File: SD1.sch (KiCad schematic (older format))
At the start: 43 parts, among them J103 JST ZH 1.5mm 1x5, J107 FPC PMS, Q101 BSS138, Q102 PDTC114EU,115, SW103 Multidirection_Switch, U102 ER-TFTM028-4, U104 CC2652P, U106 EKMC1691111, U107 MCP23017, U108 BME280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

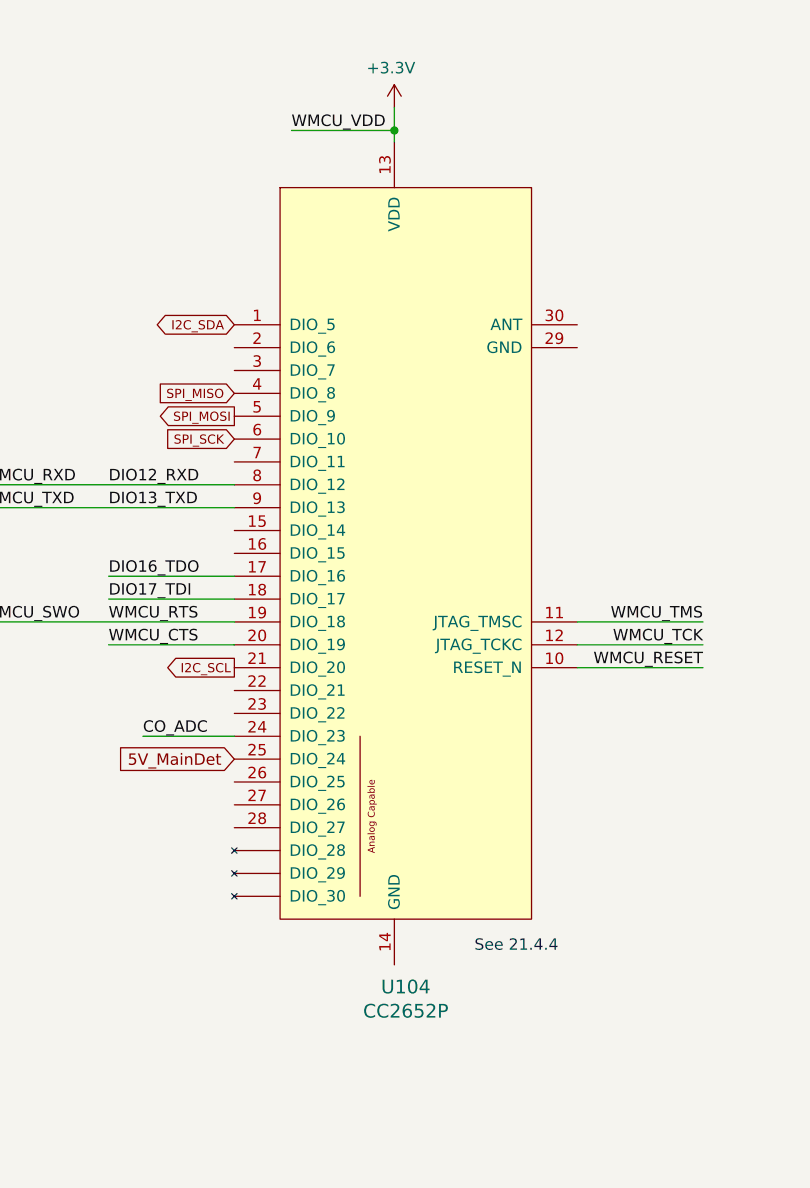
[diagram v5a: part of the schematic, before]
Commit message: PoE layout
Changed opto and fixed ref diode footprint/symbol
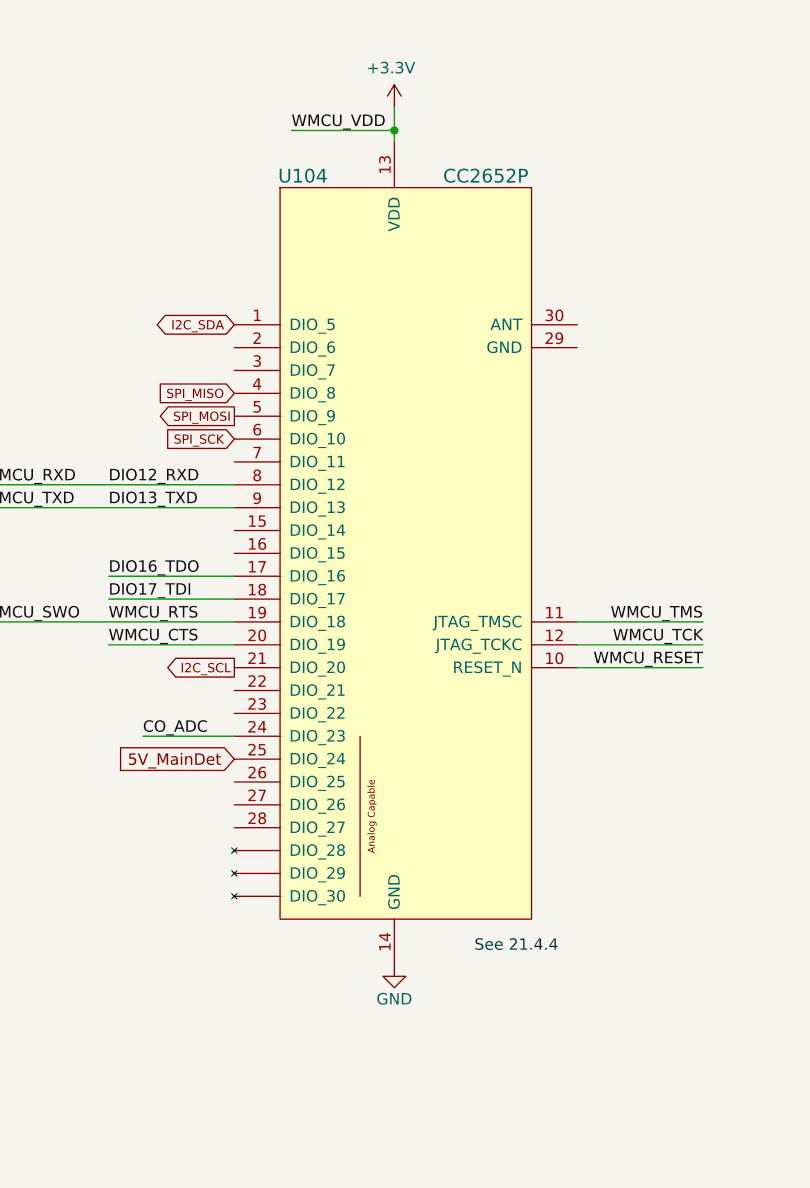
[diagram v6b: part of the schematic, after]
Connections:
- net GND: now also U104.14 (GND)
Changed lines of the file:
@@
 U 1 1 5F5DA505
 P 6500 2800
-F 0 "U104" H 6550 803 60  0000 C CNN
-F 1 "CC2652P" H 6550 697 60  0000 C CNN
+F 0 "U104" H 6100 4350 60  0000 C CNN
+F 1 "CC2652P" H 6900 4350 60  0000 C CNN
 F 2 "mylib:RF-BM-2652P2" H 6600 2900 60  0001 C CNN
 F 3 "https://www.szrfstar.com/product/237-en.html" H 7850 4300 60  0001 C CNN
@@
 P 12750 8100
 AR Path="/5E715318/6092EB6F" Ref="#PWR?"  Part="1"
-AR Path="/6092EB6F" Ref="#PWR?"  Part="1"
-F 0 "#PWR?" H 12750 7950 50  0001 C CNN
+AR Path="/6092EB6F" Ref="#PWR0203"  Part="1"
+F 0 "#PWR0203" H 12750 7950 50  0001 C CNN
 F 1 "+3.3V" H 12765 8273 50  0000 C CNN
 F 2 "" H 12750 8100 50  0001 C CNN
@@
 $EndComp
 Connection ~ 12750 8200
+$Comp
+L power:GND #PWR0204
+U 1 1 5FB1FC16
+P 6500 4700
+F 0 "#PWR0204" H 6500 4450 50  0001 C CNN
+F 1 "GND" H 6500 4550 50  0000 C CNN
+F 2 "" H 6500 4700 50  0001 C CNN
+F 3 "" H 6500 4700 50  0001 C CNN
+	1    6500 4700
+	-1   0    0    -1
+$EndComp
 $EndSCHEMATC

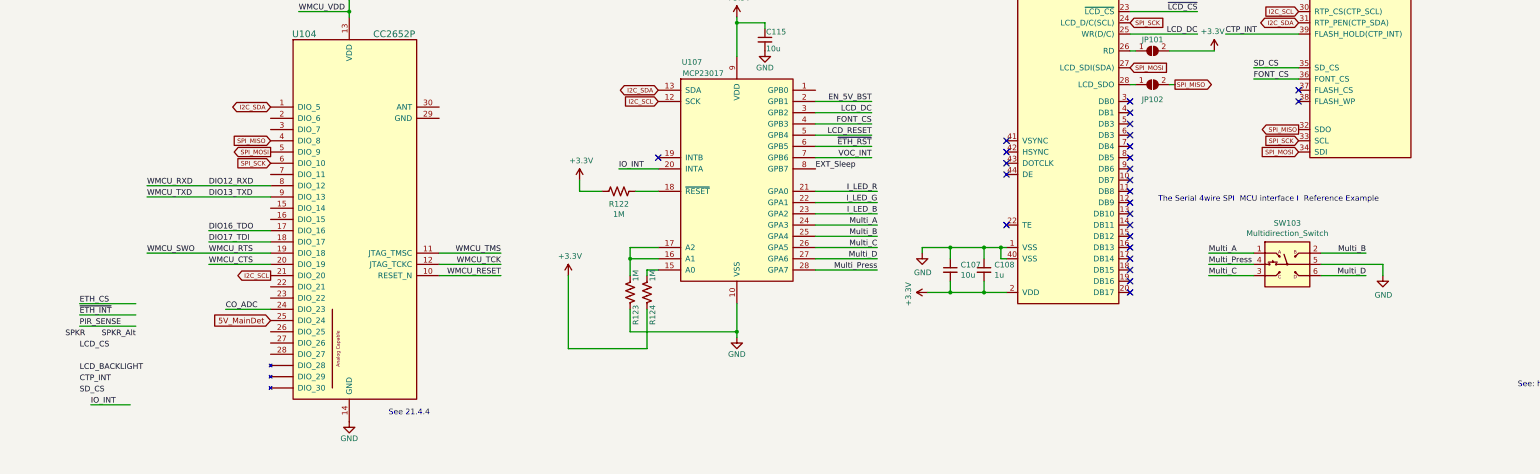
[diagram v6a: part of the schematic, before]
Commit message: Add pull down for display backlight
When h-z the backlight partially turns on. Possible to DAC this instead of PWM. Appears to use a NPN instead of a NMOS.
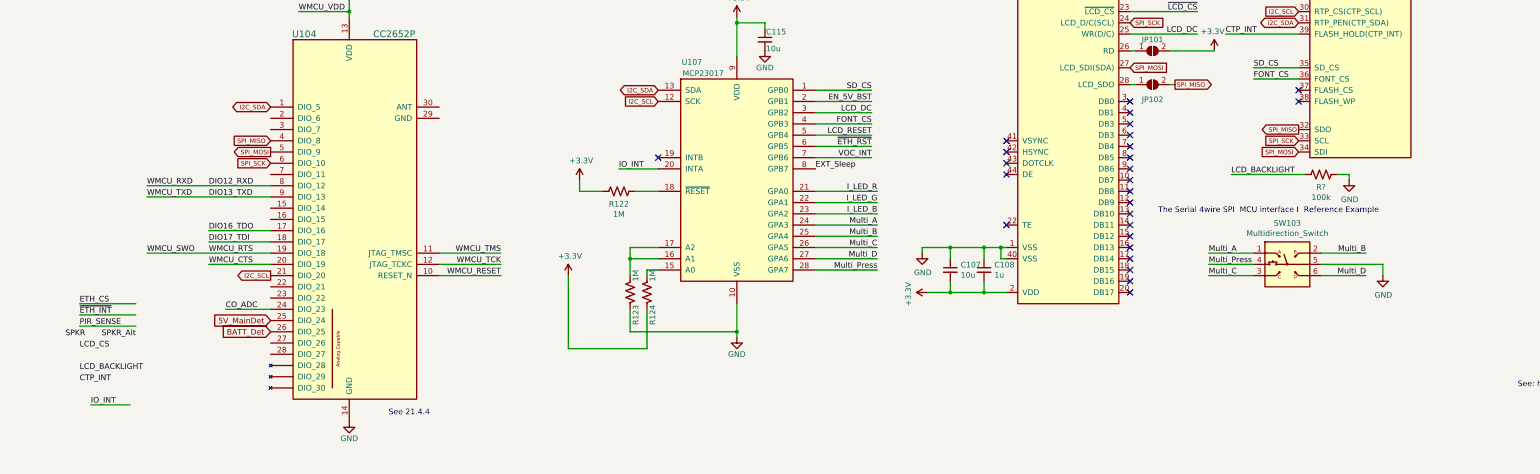
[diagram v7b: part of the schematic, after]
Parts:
- added R?: 100k, Resistor_SMD:R_0603_1608Metric, symbol Device:R_US
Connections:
- net GND: now also R?.1
- net LCD_BACKLIGHT: now also R?.2
- net SD_CS: now also U107.1 (GPB0)
- net BATT_Det: now reaches U104.26 (DIO_25)
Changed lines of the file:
@@
 	1    0    0    -1
 $EndComp
-Text Notes 13700 2750 0    50   ~ 0
+Text Notes 13700 2850 0    50   ~ 0
 The Serial 4wire SPI  MCU interface I  Reference Example
 Text GLabel 14950 1150 0    40   BiDi ~ 0
@@
 Text GLabel 13850 1700 2    40   Output ~ 0
 SPI_MISO
-Text Label 4100 4450 0    50   ~ 0
+Text Label 11150 1750 2    50   ~ 0
 SD_CS
 Text Label 11150 2050 2    50   ~ 0
@@
 Text Label 11150 1950 2    50   ~ 0
 LCD_DC
-Text Label 14300 850  0    50   ~ 0
-LCD_BACKLIGHT
 Text Label 4100 4250 0    50   ~ 0
 LCD_BACKLIGHT
@@
 Text Notes 16850 750  0    50   ~ 0
 See: https://www.buydisplay.com/download/interfacing/ER-TFT028-4_CTP_Interfacing.pdf
-Wire Wire Line
-	14300 850  14950 850
 Text Label 14550 1650 0    50   ~ 0
 FONT_CS
@@
 	-1   0    0    -1
 $EndComp
+Wire Wire Line
+	11150 1750 10650 1750
+Text GLabel 5800 3900 0    50   Input ~ 0
+BATT_Det
+Wire Wire Line
+	14300 850  14950 850
+Text Label 14300 850  0    50   ~ 0
+LCD_BACKLIGHT
+Wire Wire Line
+	14350 2500 15000 2500
+Text Label 14350 2500 0    50   ~ 0
+LCD_BACKLIGHT
+$Comp
+L Device:R_US R?
+U 1 1 5FC4D37E
+P 15150 2500
+AR Path="/5E360A9B/5FC4D37E" Ref="R?"  Part="1"
+AR Path="/5FC4D37E" Ref="R?"  Part="1"
+AR Path="/5E5C8043/5E5C885F/5FC4D37E" Ref="R?"  Part="1"
+AR Path="/5E5C8043/5E9EE9F0/5FC4D37E" Ref="R?"  Part="1"
+AR Path="/5E5C8043/5EA19CBA/5FC4D37E" Ref="R?"  Part="1"
+AR Path="/5E5C8043/5E49A000/5FC4D37E" Ref="R?"  Part="1"
+AR Path="/5E5C8043/5EAB3002/5FC4D37E" Ref="R?"  Part="1"
+AR Path="/5E5C8043/5FC4D37E" Ref="R?"  Part="1"
+AR Path="/5E715318/5FC4D37E" Ref="R?"  Part="1"
+AR Path="/5FAF778C/5FC4D37E" Ref="R?"  Part="1"
+AR Path="/5FCEDB09/5FAC6B33/5FC4D37E" Ref="R?"  Part="1"
+F 0 "R?" V 15263 2500 50  0000 C CNN
+F 1 "100k" V 15354 2500 50  0000 C CNN
+F 2 "Resistor_SMD:R_0603_1608Metric" V 15190 2490 50  0001 C CNN
+F 3 "~" H 15150 2500 50  0001 C CNN
+F 4 "RC0603FR-07100KL" H 15150 2500 50  0001 C CNN "MPN"
+F 5 "311-100KHRCT-ND" H 15150 2500 50  0001 C CNN "Digikey"
+F 6 "RES SMD 100K OHM 1% 1/10W 0603" H 15150 2500 50  0001 C CNN "Note"
+	1    15150 2500
+	0    1    1    0
+$EndComp
+$Comp
+L power:GND #PWR?
+U 1 1 5FC5AFAE
+P 15400 2550
+F 0 "#PWR?" H 15400 2300 50  0001 C CNN
+F 1 "GND" H 15405 2377 50  0000 C CNN
+F 2 "" H 15400 2550 50  0001 C CNN
+F 3 "" H 15400 2550 50  0001 C CNN
+	1    15400 2550
+	1    0    0    -1
+$EndComp
+Wire Wire Line
+	15300 2500 15400 2500
+Wire Wire Line
+	15400 2500 15400 2550
 $EndSCHEMATC

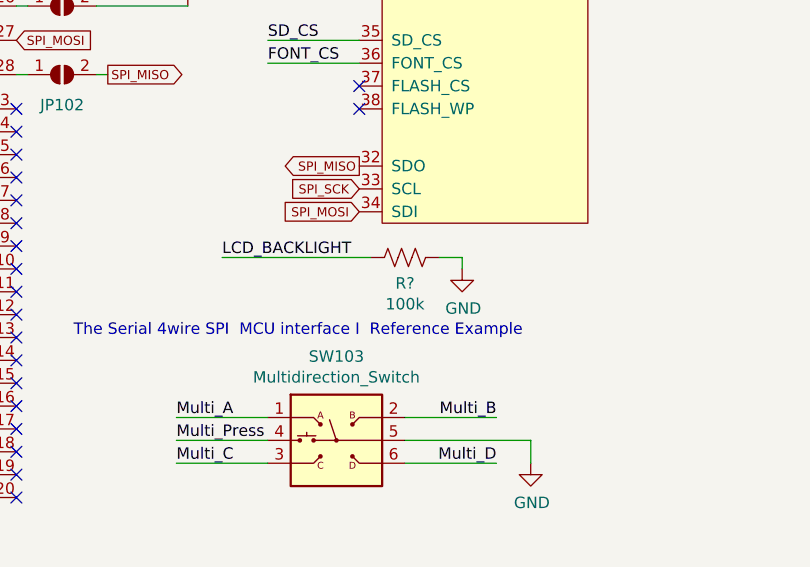
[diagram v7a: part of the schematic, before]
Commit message: Added battery charger schematic
Annotated
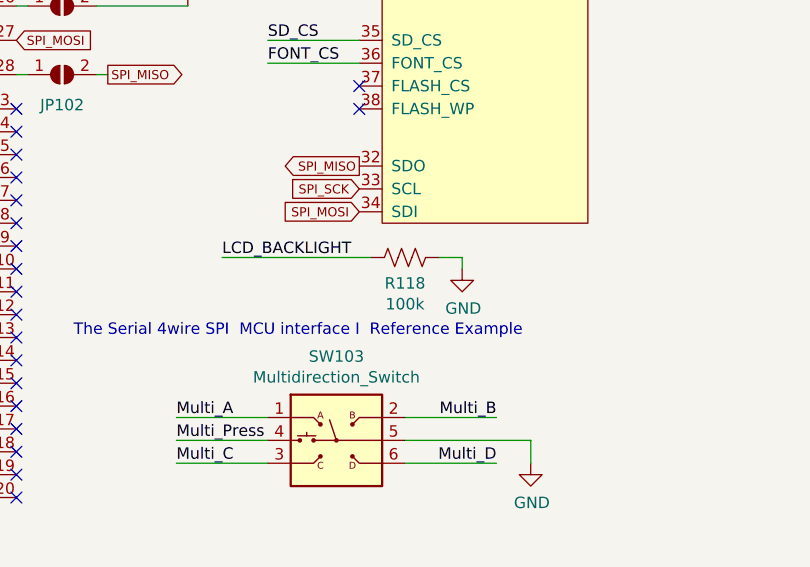
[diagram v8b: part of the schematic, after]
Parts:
- gave numbers to parts that had none: 1
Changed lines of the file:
@@
 P 15150 2500
 AR Path="/5E360A9B/5FC4D37E" Ref="R?"  Part="1"
-AR Path="/5FC4D37E" Ref="R?"  Part="1"
+AR Path="/5FC4D37E" Ref="R118"  Part="1"
 AR Path="/5E5C8043/5E5C885F/5FC4D37E" Ref="R?"  Part="1"
 AR Path="/5E5C8043/5E9EE9F0/5FC4D37E" Ref="R?"  Part="1"
@@
 AR Path="/5FAF778C/5FC4D37E" Ref="R?"  Part="1"
 AR Path="/5FCEDB09/5FAC6B33/5FC4D37E" Ref="R?"  Part="1"
-F 0 "R?" V 15263 2500 50  0000 C CNN
+F 0 "R118" V 15263 2500 50  0000 C CNN
 F 1 "100k" V 15354 2500 50  0000 C CNN
 F 2 "Resistor_SMD:R_0603_1608Metric" V 15190 2490 50  0001 C CNN
@@
 $EndComp
 $Comp
-L power:GND #PWR?
+L power:GND #PWR0205
 U 1 1 5FC5AFAE
 P 15400 2550
-F 0 "#PWR?" H 15400 2300 50  0001 C CNN
+F 0 "#PWR0205" H 15400 2300 50  0001 C CNN
 F 1 "GND" H 15405 2377 50  0000 C CNN
 F 2 "" H 15400 2550 50  0001 C CNN
